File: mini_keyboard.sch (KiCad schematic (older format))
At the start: 42 parts, among them SW1 SW_DIP_x01, SW10 SW_DIP_x01, SW11 SW_DIP_x01, SW12 SW_DIP_x01, SW13 SW_DIP_x01, SW14 SW_DIP_x01, SW15 SW_DIP_x01, SW16 SW_DIP_x01, SW17 SW_DIP_x01, SW18 SW_DIP_x01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

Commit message: rules check passed
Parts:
- gave numbers to parts that had none: 2
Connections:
- net 5V: no longer J1.4 (Pin_4)
- net GND: no longer J1.5 (Pin_5)
- net SW: no longer J1.1 (Pin_1)
- net VRX: no longer J1.2 (Pin_2)
- net VRY: no longer J1.3 (Pin_3)
- net at U1.11 (B4): now also J1.1 (Pin_1)
- net at U1.12 (B5): now also J1.2 (Pin_2)
- net at U1.13 (B6): now also J1.3 (Pin_3)
- net at U1.21 (VCC): now also J1.4 (Pin_4)
- net at U1.23 (GND): now also J1.5 (Pin_5)
- no-connect marks 0 -> 10
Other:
- moved on the sheet: J1
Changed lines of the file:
@@
 col4
 $Comp
-L Connector:Conn_01x05_Male J?
-U 1 1 60183F68
-P 6000 7400
-F 0 "J?" H 6108 7781 50  0000 C CNN
-F 1 "Conn_01x05_Male" H 6108 7690 50  0000 C CNN
-F 2 "" H 6000 7400 50  0001 C CNN
-F 3 "~" H 6000 7400 50  0001 C CNN
-	1    6000 7400
-	0    -1   -1   0
-$EndComp
-$Comp
-L promicro:ProMicro U?
+L promicro:ProMicro U1
 U 1 1 60148DE3
 P 5900 6400
-F 0 "U?" H 5900 7437 60  0000 C CNN
+F 0 "U1" H 5900 7437 60  0000 C CNN
 F 1 "ProMicro" H 5900 7331 60  0000 C CNN
 F 2 "" H 6000 5350 60  0000 C CNN
@@
 Text Label 5200 6450 2    50   ~ 0
 row5
-Text Label 6200 7200 1    50   ~ 0
+$Comp
+L Connector:Conn_01x05_Male J1
+U 1 1 60183F68
+P 7650 6500
+F 0 "J1" H 7758 6881 50  0000 C CNN
+F 1 "Conn_01x05_Male" H 7758 6790 50  0000 C CNN
+F 2 "" H 7650 6500 50  0001 C CNN
+F 3 "~" H 7650 6500 50  0001 C CNN
+	1    7650 6500
+	0    -1   -1   0
+$EndComp
+Text Label 7850 5450 1    50   ~ 0
 GND
-Text Label 6100 7200 1    50   ~ 0
+Text Label 7750 5450 1    50   ~ 0
 5V
-Text Label 6000 7200 1    50   ~ 0
+Text Label 7650 5450 1    50   ~ 0
 VRY
-Text Label 5900 7200 1    50   ~ 0
+Text Label 7550 5450 1    50   ~ 0
 VRX
-Text Label 5800 7200 1    50   ~ 0
+Text Label 7450 5450 1    50   ~ 0
 SW
+Wire Wire Line
+	7850 5750 7450 5750
+Wire Wire Line
+	7750 5950 7450 5950
+Wire Wire Line
+	7850 5750 7850 6300
+Wire Wire Line
+	7750 5950 7750 6300
+Wire Wire Line
+	7650 6300 7650 6000
+Wire Wire Line
+	7650 6000 6850 6000
+Wire Wire Line
+	6850 6000 6850 6750
+Wire Wire Line
+	6850 6750 6600 6750
+Wire Wire Line
+	7550 6300 7550 6050
+Wire Wire Line
+	7550 6050 6900 6050
+Wire Wire Line
+	6900 6050 6900 6900
+Wire Wire Line
+	6900 6900 5200 6900
+Wire Wire Line
+	5200 6900 5200 6750
+Wire Wire Line
+	7450 6300 7450 6100
+Wire Wire Line
+	7450 6100 6950 6100
+Wire Wire Line
+	6950 6100 6950 6950
+Wire Wire Line
+	6950 6950 5150 6950
+Wire Wire Line
+	5150 6950 5150 6650
+Wire Wire Line
+	5150 6650 5200 6650
+NoConn ~ 6600 6650
+NoConn ~ 6600 6550
+NoConn ~ 6600 6450
+NoConn ~ 6600 5850
+NoConn ~ 6600 5650
+NoConn ~ 5200 6550
+NoConn ~ 5200 5950
+NoConn ~ 5200 5850
+NoConn ~ 5200 5750
+NoConn ~ 5200 5650
+$Comp
+L power:PWR_FLAG #FLG0101
+U 1 1 602049E6
+P 7450 5750
+F 0 "#FLG0101" H 7450 5825 50  0001 C CNN
+F 1 "PWR_FLAG" H 7450 5923 50  0000 C CNN
+F 2 "" H 7450 5750 50  0001 C CNN
+F 3 "~" H 7450 5750 50  0001 C CNN
+	1    7450 5750
+	1    0    0    -1
+$EndComp
+Connection ~ 7450 5750
+Wire Wire Line
+	7450 5750 6600 5750
+$Comp
+L power:PWR_FLAG #FLG0102
+U 1 1 60205AA3
+P 7450 5950
+F 0 "#FLG0102" H 7450 6025 50  0001 C CNN
+F 1 "PWR_FLAG" H 7450 6123 50  0000 C CNN
+F 2 "" H 7450 5950 50  0001 C CNN
+F 3 "~" H 7450 5950 50  0001 C CNN
+	1    7450 5950
+	1    0    0    -1
+$EndComp
+Connection ~ 7450 5950
+Wire Wire Line
+	7450 5950 6600 5950
 $EndSCHEMATC

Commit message: promicro footprint correct added
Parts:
- J1: footprint (none) -> Connector_PinHeader_2.54mm:PinHeader_1x05_P2.54mm_Vertical
- U1: footprint (none) -> promicro:ProMicro; symbol promicro:ProMicro -> mini_keyboard-rescue:ProMicro-promicro
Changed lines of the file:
@@
 col4
 $Comp
-L promicro:ProMicro U1
+L mini_keyboard-rescue:ProMicro-promicro U1
 U 1 1 60148DE3
 P 5900 6400
 F 0 "U1" H 5900 7437 60  0000 C CNN
 F 1 "ProMicro" H 5900 7331 60  0000 C CNN
-F 2 "" H 6000 5350 60  0000 C CNN
+F 2 "promicro:ProMicro" H 6000 5350 60  0001 C CNN
 F 3 "" H 6000 5350 60  0000 C CNN
 	1    5900 6400
@@
 F 0 "J1" H 7758 6881 50  0000 C CNN
 F 1 "Conn_01x05_Male" H 7758 6790 50  0000 C CNN
-F 2 "" H 7650 6500 50  0001 C CNN
+F 2 "Connector_PinHeader_2.54mm:PinHeader_1x05_P2.54mm_Vertical" H 7650 6500 50  0001 C CNN
 F 3 "~" H 7650 6500 50  0001 C CNN
 	1    7650 6500

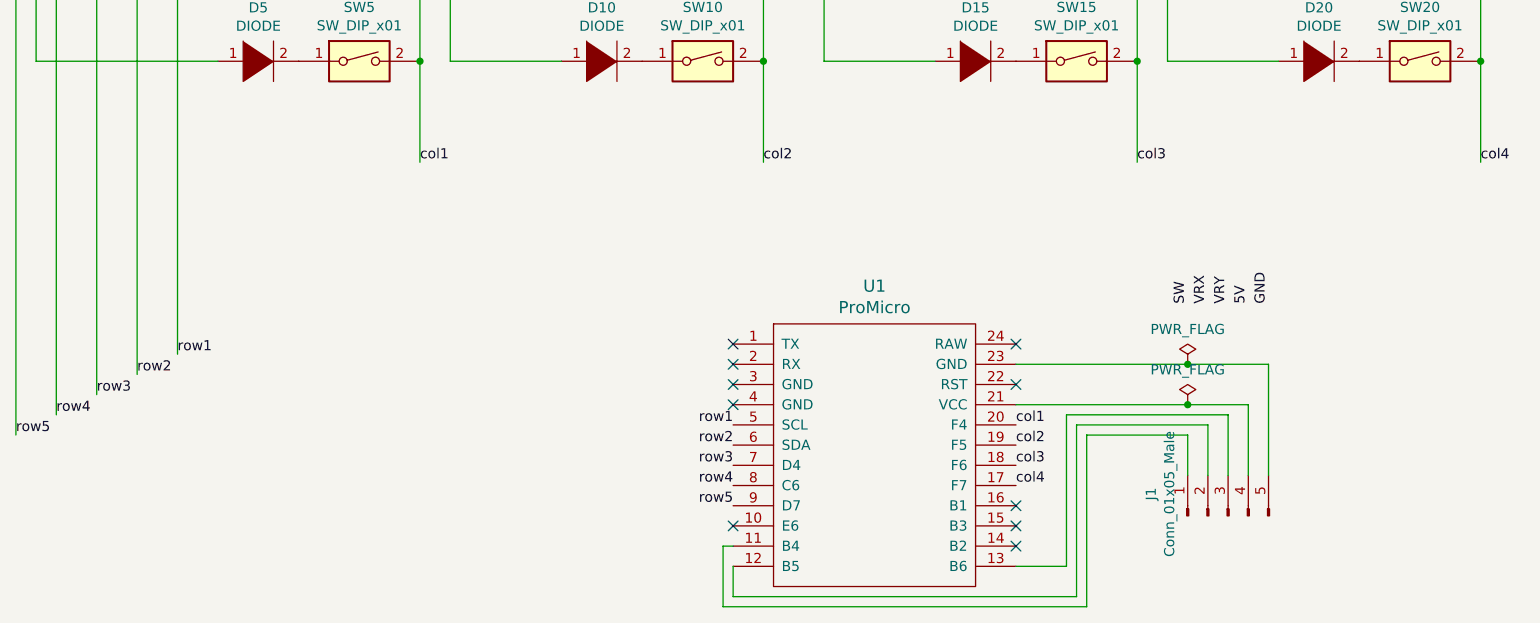
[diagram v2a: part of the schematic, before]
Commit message: made back and front cables
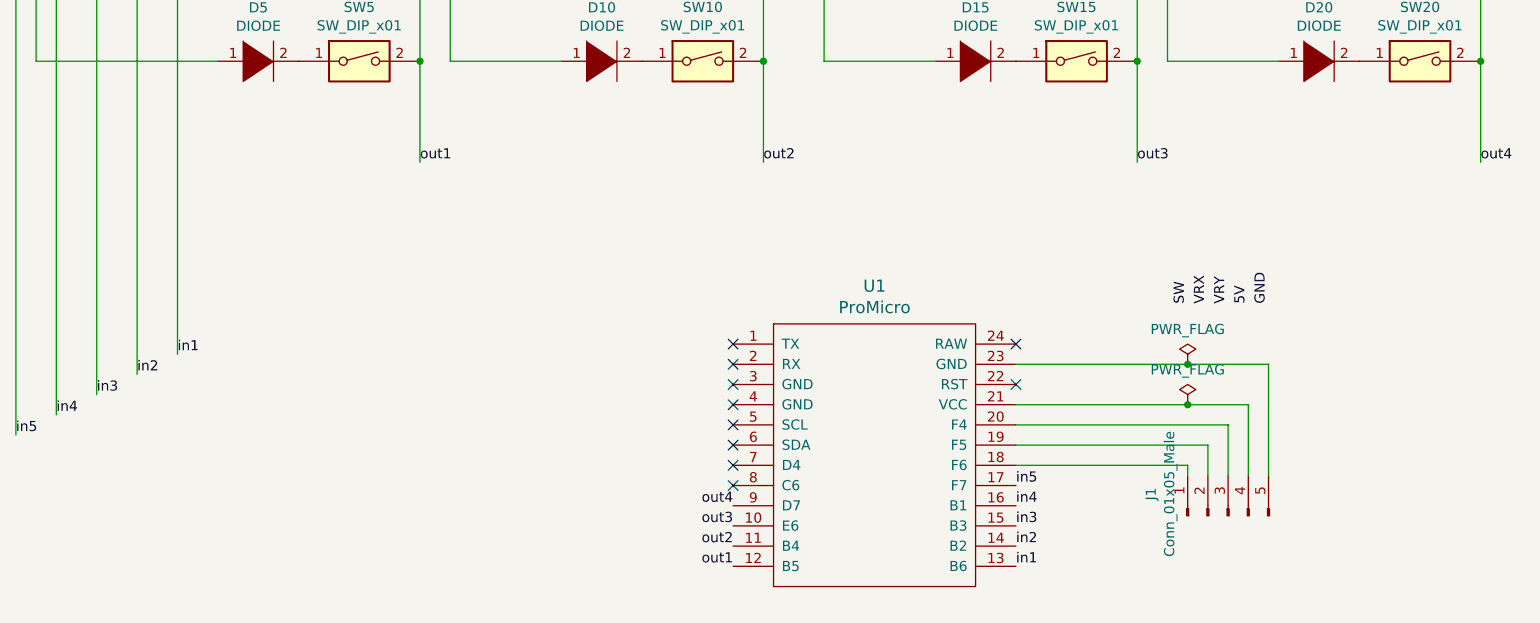
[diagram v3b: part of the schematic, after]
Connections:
- net out3: now reaches U1.10 (E6)
- net out3: now also SW11.2, SW12.2, SW13.2, SW14.2, SW15.2
- net at J1.1 (Pin_1): now also U1.18 (F6); no longer U1.11 (B4)
- net at J1.2 (Pin_2): now also U1.19 (F5); no longer U1.12 (B5)
- net at J1.3 (Pin_3): now also U1.20 (F4); no longer U1.13 (B6)
- net in2: now reaches U1.14 (B2)
- net in2: now also D12.1 (K), D17.1 (K), D2.1 (K), D7.1 (K)
- net in3: now reaches U1.15 (B3)
- net in3: now also D13.1 (K), D18.1 (K), D3.1 (K), D8.1 (K)
- net in4: now reaches U1.16 (B1)
- net in4: now also D14.1 (K), D19.1 (K), D4.1 (K), D9.1 (K)
- net col1 renamed out1
- net out1: now also U1.12 (B5); no longer U1.20 (F4)
- net col2 renamed out2
- net out2: now also U1.11 (B4); no longer U1.19 (F5)
- removed net col3: SW11.2, SW12.2, SW13.2, SW14.2, SW15.2, U1.18 (F6)
- net col4 renamed out4
- net out4: now also U1.9 (D7); no longer U1.17 (F7)
- net row1 renamed in1
- net in1: now also U1.13 (B6); no longer U1.5 (SCL)
- removed net row2: D12.1 (K), D17.1 (K), D2.1 (K), D7.1 (K), U1.6 (SDA)
- removed net row3: D13.1 (K), D18.1 (K), D3.1 (K), D8.1 (K), U1.7 (D4)
- removed net row4: D14.1 (K), D19.1 (K), D4.1 (K), D9.1 (K), U1.8 (C6)
- net row5 renamed in5
- net in5: now also U1.17 (F7); no longer U1.9 (D7)
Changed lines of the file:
@@
 $EndComp
 Text Label 2450 5700 0    50   ~ 0
-row1
+in1
 Text Label 2250 5800 0    50   ~ 0
-row2
+in2
 Text Label 2050 5900 0    50   ~ 0
-row3
+in3
 Text Label 1850 6000 0    50   ~ 0
-row4
+in4
 Text Label 1650 6100 0    50   ~ 0
-row5
+in5
 Wire Wire Line
 	3650 4250 3650 4750
@@
 Connection ~ 8900 4250
 Text Label 3650 4750 0    50   ~ 0
-col1
+out1
 Text Label 5350 4750 0    50   ~ 0
-col2
+out2
 Text Label 7200 4750 0    50   ~ 0
-col3
+out3
 Text Label 8900 4750 0    50   ~ 0
-col4
-$Comp
-L mini_keyboard-rescue:ProMicro-promicro U1
-U 1 1 60148DE3
-P 5900 6400
-F 0 "U1" H 5900 7437 60  0000 C CNN
-F 1 "ProMicro" H 5900 7331 60  0000 C CNN
-F 2 "promicro:ProMicro" H 6000 5350 60  0001 C CNN
-F 3 "" H 6000 5350 60  0000 C CNN
-	1    5900 6400
-	1    0    0    -1
-$EndComp
-Text Label 6600 6050 0    50   ~ 0
-col1
-Text Label 6600 6150 0    50   ~ 0
-col2
-Text Label 6600 6250 0    50   ~ 0
-col3
+out4
+Text Label 5200 6750 2    50   ~ 0
+out1
+Text Label 5200 6650 2    50   ~ 0
+out2
+Text Label 5200 6550 2    50   ~ 0
+out3
+Text Label 5200 6450 2    50   ~ 0
+out4
+Text Label 6600 6750 0    50   ~ 0
+in1
+Text Label 6600 6550 0    50   ~ 0
+in3
+Text Label 6600 6450 0    50   ~ 0
+in4
 Text Label 6600 6350 0    50   ~ 0
-col4
-Text Label 5200 6050 2    50   ~ 0
-row1
-Text Label 5200 6150 2    50   ~ 0
-row2
-Text Label 5200 6250 2    50   ~ 0
-row3
-Text Label 5200 6350 2    50   ~ 0
-row4
-Text Label 5200 6450 2    50   ~ 0
-row5
+in5
 $Comp
 L Connector:Conn_01x05_Male J1
@@
 Wire Wire Line
 	7750 5950 7750 6300
-Wire Wire Line
-	7650 6300 7650 6000
-Wire Wire Line
-	7650 6000 6850 6000
-Wire Wire Line
-	6850 6000 6850 6750
-Wire Wire Line
-	6850 6750 6600 6750
-Wire Wire Line
-	7550 6300 7550 6050
-Wire Wire Line
-	7550 6050 6900 6050
-Wire Wire Line
-	6900 6050 6900 6900
-Wire Wire Line
-	6900 6900 5200 6900
-Wire Wire Line
-	5200 6900 5200 6750
-Wire Wire Line
-	7450 6300 7450 6100
-Wire Wire Line
-	7450 6100 6950 6100
-Wire Wire Line
-	6950 6100 6950 6950
-Wire Wire Line
-	6950 6950 5150 6950
-Wire Wire Line
-	5150 6950 5150 6650
-Wire Wire Line
-	5150 6650 5200 6650
-NoConn ~ 6600 6650
-NoConn ~ 6600 6550
-NoConn ~ 6600 6450
 NoConn ~ 6600 5850
 NoConn ~ 6600 5650
-NoConn ~ 5200 6550
 NoConn ~ 5200 5950
 NoConn ~ 5200 5850
@@
 Wire Wire Line
 	7450 5950 6600 5950
+Wire Wire Line
+	7650 6300 7650 6050
+Wire Wire Line
+	7650 6050 6600 6050
+Wire Wire Line
+	7550 6300 7550 6150
+Wire Wire Line
+	7550 6150 6600 6150
+Wire Wire Line
+	7450 6300 7450 6250
+Wire Wire Line
+	7450 6250 6600 6250
+$Comp
+L mini_keyboard-rescue:ProMicro-promicro U1
+U 1 1 60148DE3
+P 5900 6400
+F 0 "U1" H 5900 7437 60  0000 C CNN
+F 1 "ProMicro" H 5900 7331 60  0000 C CNN
+F 2 "promicro:ProMicro" H 6000 5350 60  0001 C CNN
+F 3 "" H 6000 5350 60  0000 C CNN
+	1    5900 6400
+	1    0    0    -1
+$EndComp
+Text Label 6600 6650 0    50   ~ 0
+in2
+NoConn ~ 5200 6350
+NoConn ~ 5200 6250
+NoConn ~ 5200 6150
+NoConn ~ 5200 6050
 $EndSCHEMATC

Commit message: Thick lines
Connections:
- net out1: now also U1.9 (D7); no longer U1.12 (B5)
- net out2: now also U1.10 (E6); no longer U1.11 (B4)
- net out3: now also U1.11 (B4); no longer U1.10 (E6)
- net out4: now also U1.12 (B5); no longer U1.9 (D7)
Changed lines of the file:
@@
 Text Label 8900 4750 0    50   ~ 0
-out4
-Text Label 5200 6750 2    50   ~ 0
-out1
-Text Label 5200 6650 2    50   ~ 0
-out2
-Text Label 5200 6550 2    50   ~ 0
-out3
-Text Label 5200 6450 2    50   ~ 0
 out4
 Text Label 6600 6750 0    50   ~ 0
@@
 NoConn ~ 5200 6150
 NoConn ~ 5200 6050
+Text Label 5200 6450 2    50   ~ 0
+out1
+Text Label 5200 6550 2    50   ~ 0
+out2
+Text Label 5200 6650 2    50   ~ 0
+out3
+Text Label 5200 6750 2    50   ~ 0
+out4
 $EndSCHEMATC

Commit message: Made out on right A_ ports
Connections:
- net out1: now also U1.7 (D4); no longer U1.9 (D7)
- net out2: now also U1.9 (D7); no longer U1.10 (E6)
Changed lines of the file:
@@
 Text Label 6600 6650 0    50   ~ 0
 in2
-NoConn ~ 5200 6350
-NoConn ~ 5200 6250
 NoConn ~ 5200 6150
 NoConn ~ 5200 6050
+Text Label 5200 6250 2    50   ~ 0
+out1
 Text Label 5200 6450 2    50   ~ 0
-out1
-Text Label 5200 6550 2    50   ~ 0
 out2
 Text Label 5200 6650 2    50   ~ 0
@@
 Text Label 5200 6750 2    50   ~ 0
 out4
+NoConn ~ 5200 6350
+NoConn ~ 5200 6550
 $EndSCHEMATC

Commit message: minor change2
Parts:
- SW1, SW11, SW16, SW6: footprint Button_Switch_Keyboard:SW_Cherry_MX_1.00u_Plate -> Button_Switch_Keyboard:SW_Cherry_MX_1.50u_Plate
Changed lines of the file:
@@
 F 0 "SW6" H 5050 2517 50  0000 C CNN
 F 1 "SW_DIP_x01" H 5050 2426 50  0000 C CNN
-F 2 "Button_Switch_Keyboard:SW_Cherry_MX_1.00u_Plate" H 5050 2250 50  0001 C CNN
+F 2 "Button_Switch_Keyboard:SW_Cherry_MX_1.50u_Plate" H 5050 2250 50  0001 C CNN
 F 3 "~" H 5050 2250 50  0001 C CNN
 	1    5050 2250
@@
 F 0 "SW1" H 3350 2517 50  0000 C CNN
 F 1 "SW_DIP_x01" H 3350 2426 50  0000 C CNN
-F 2 "Button_Switch_Keyboard:SW_Cherry_MX_1.00u_Plate" H 3350 2250 50  0001 C CNN
+F 2 "Button_Switch_Keyboard:SW_Cherry_MX_1.50u_Plate" H 3350 2250 50  0001 C CNN
 F 3 "~" H 3350 2250 50  0001 C CNN
 	1    3350 2250
@@
 F 0 "SW16" H 8600 2517 50  0000 C CNN
 F 1 "SW_DIP_x01" H 8600 2426 50  0000 C CNN
-F 2 "Button_Switch_Keyboard:SW_Cherry_MX_1.00u_Plate" H 8600 2250 50  0001 C CNN
+F 2 "Button_Switch_Keyboard:SW_Cherry_MX_1.50u_Plate" H 8600 2250 50  0001 C CNN
 F 3 "~" H 8600 2250 50  0001 C CNN
 	1    8600 2250
@@
 F 0 "SW11" H 6900 2517 50  0000 C CNN
 F 1 "SW_DIP_x01" H 6900 2426 50  0000 C CNN
-F 2 "Button_Switch_Keyboard:SW_Cherry_MX_1.00u_Plate" H 6900 2250 50  0001 C CNN
+F 2 "Button_Switch_Keyboard:SW_Cherry_MX_1.50u_Plate" H 6900 2250 50  0001 C CNN
 F 3 "~" H 6900 2250 50  0001 C CNN
 	1    6900 2250
